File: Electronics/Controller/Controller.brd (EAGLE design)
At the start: 190 x 90 mm, 20 parts, among them Q1 IRFD9014, U1 GY-521MPU6050, X1 Battery, X2 Switch

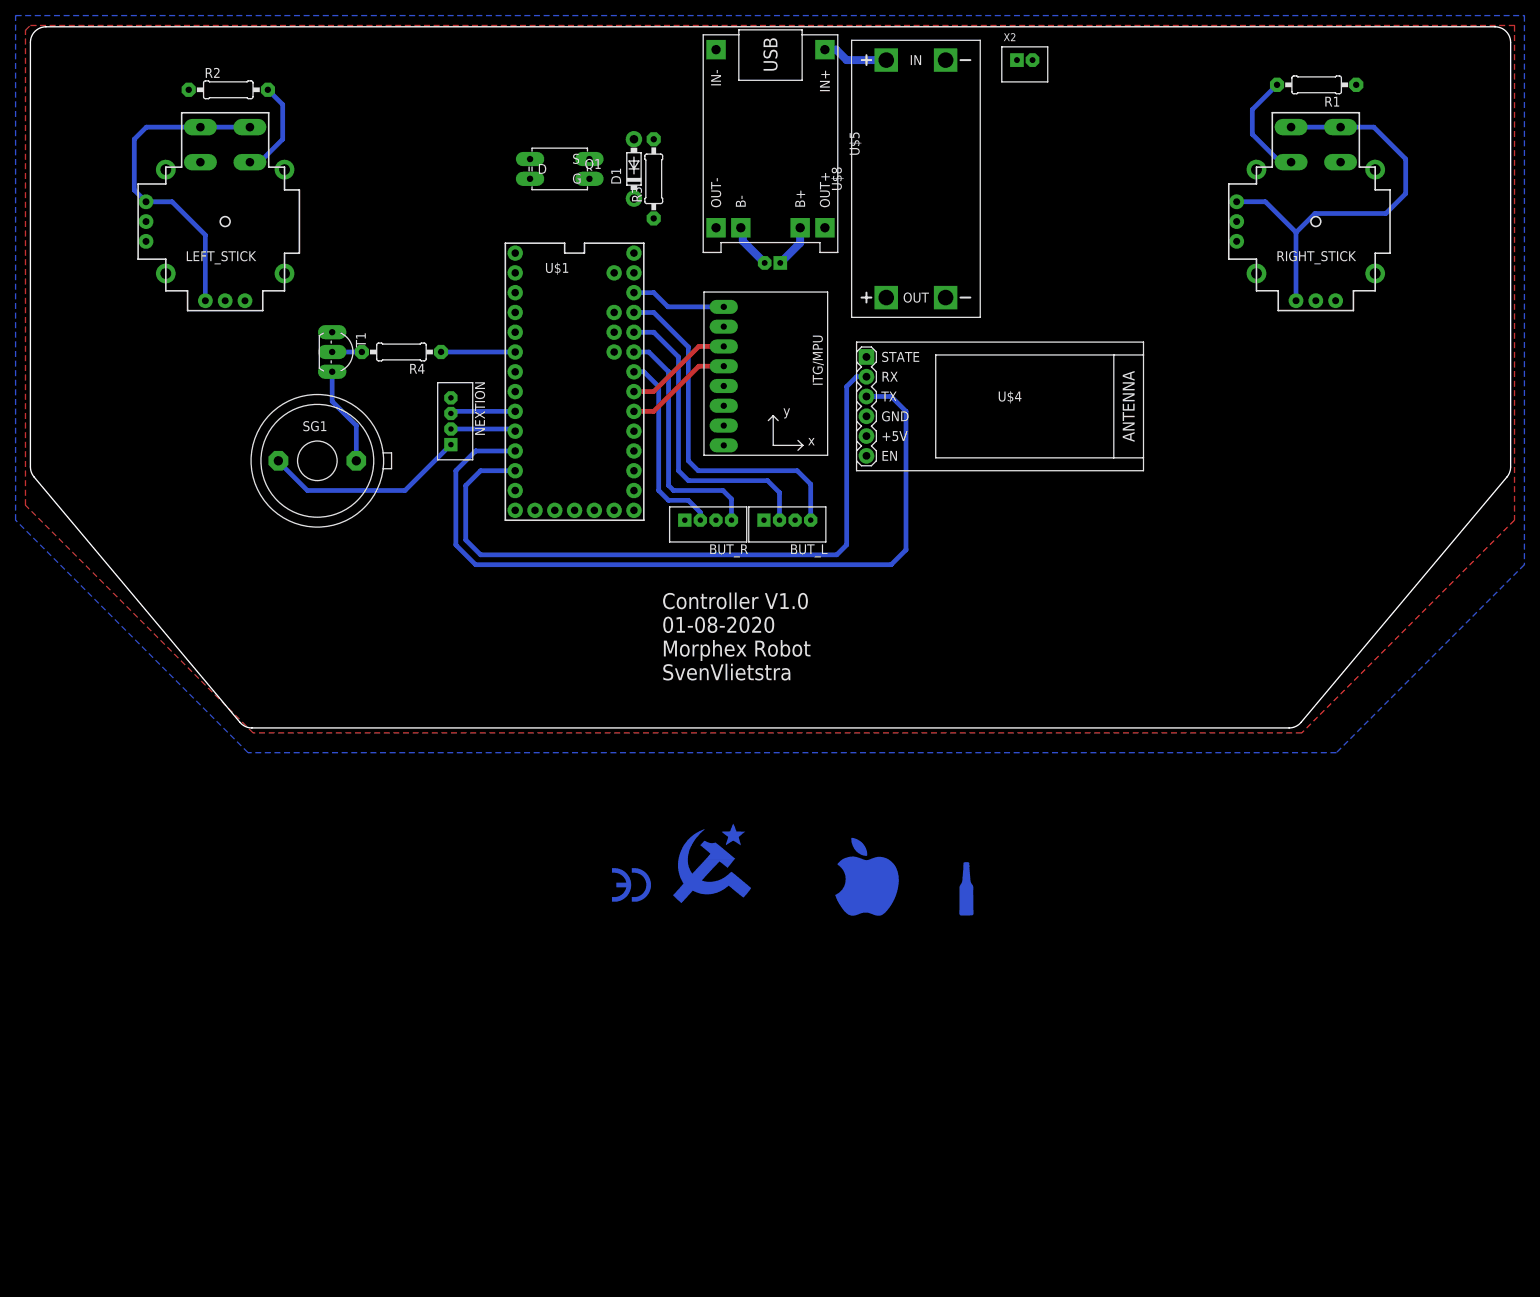
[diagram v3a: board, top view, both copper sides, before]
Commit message: Completed all routes
Completed all routes and changed the P-Channel mosfet to a NDP6020P
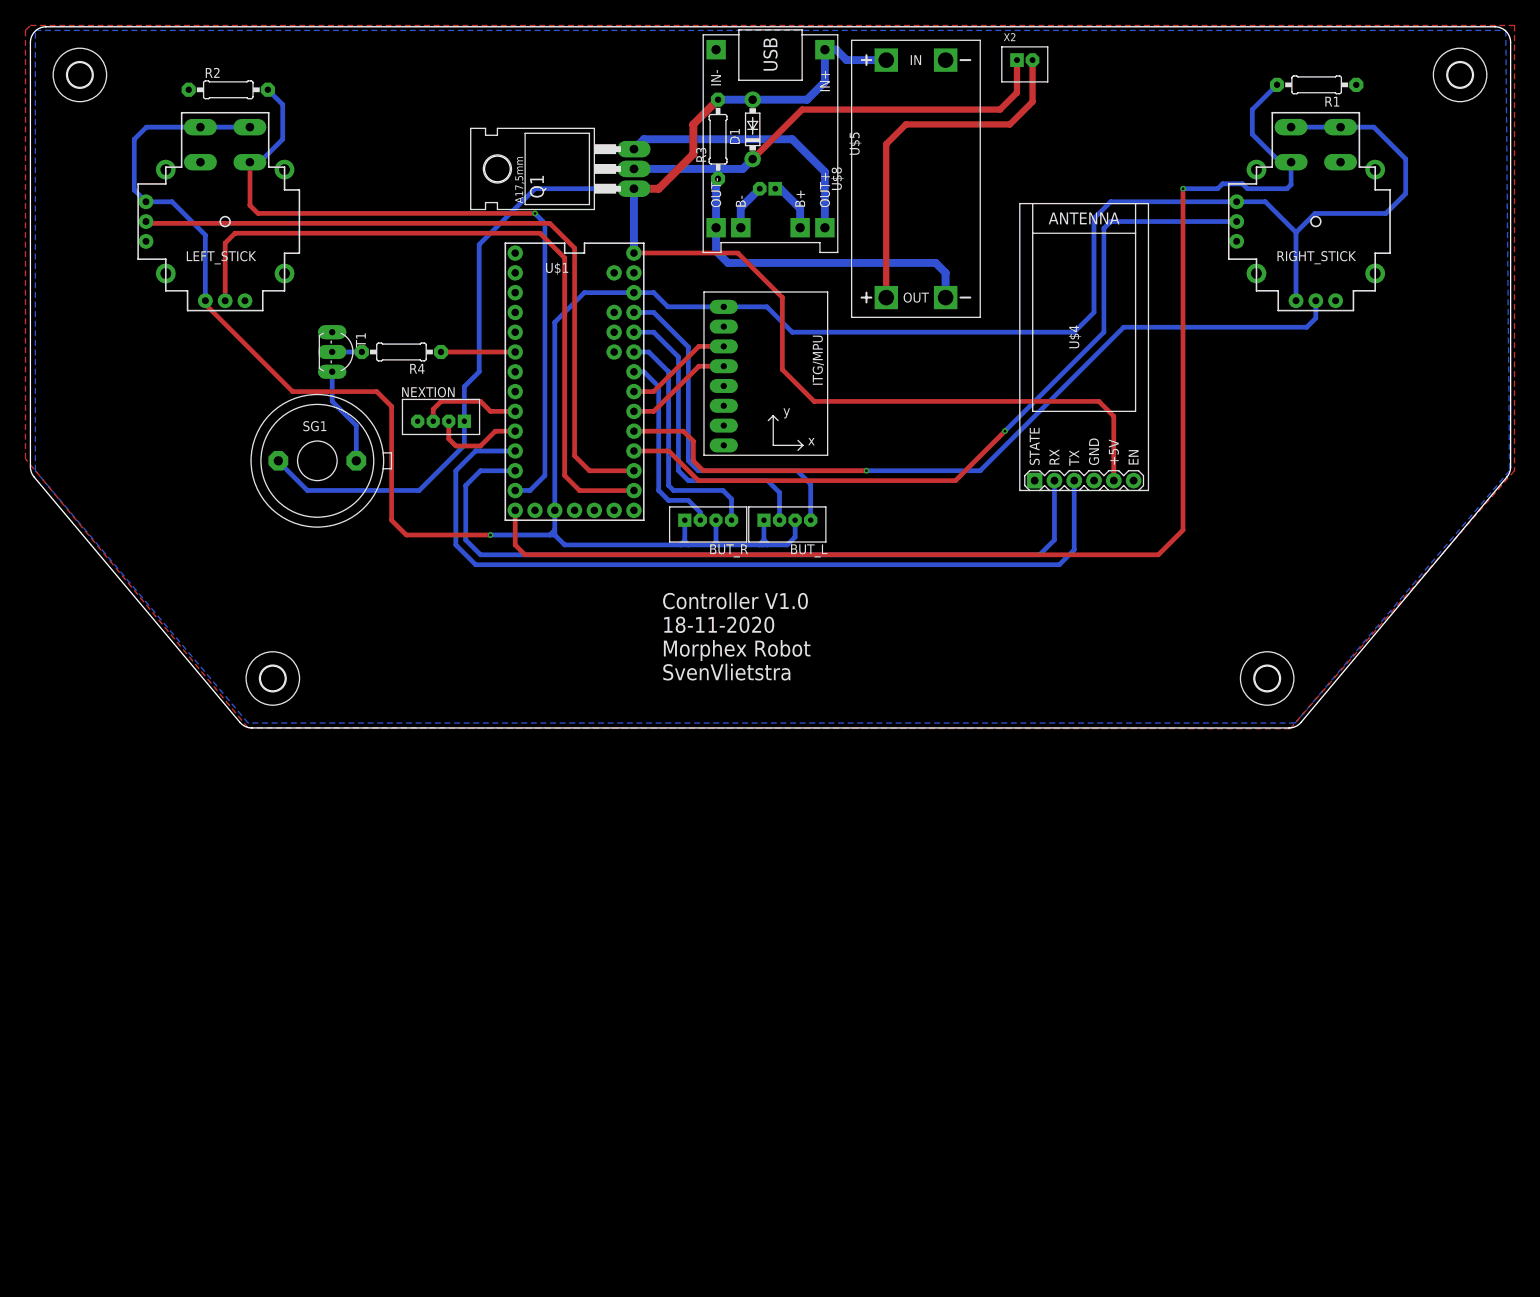
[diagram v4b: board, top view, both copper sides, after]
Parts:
- added U$2, U$3, U$6, U$7: (no value), holes:3,2
- Q1: value IRFD9014 -> (none); device transistor-small-signal:C370-01 -> transistor-power:TO220BH
- moved D1 16.1 mm to (92.7, 76.8)
- moved U$4 13.2 mm to (135.3, 48.9), turned to 0 degrees
- moved R3 9.69 mm to (88.3, 75.6)
- moved X1 9.55 mm to (94.6, 69.2)
- moved Q1 3.18 mm to (71.1, 71.8), turned to 90 degrees
- moved NEXTION 1.27 mm to (52.7, 39.4), turned to 0 degrees
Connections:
- new net SW2: R1.2, RIGHT_STICK.B2A, RIGHT_STICK.B2B, U$1.12
- net N$4: no longer Q1.D1
- net SW1: no longer R1.2, RIGHT_STICK.B2A, RIGHT_STICK.B2B, U$1.12
- net X-AXIS1: now also U$1.15/A1; no longer U$1.14/A0
- net Y-AXIS1: now also U$1.14/A0; no longer U$1.15/A1
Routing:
- net +3V3: track 109.2 -> 343.3 mm, vias 0 -> 1
- net +5V: track 34.6 -> 214.5 mm
- net SW2: track 0.00 -> 167.4 mm, vias 0 -> 1
- net Y-AXIS2: track 0.00 -> 101.5 mm, vias 0 -> 1
- net X-AXIS2: track 0.00 -> 100.5 mm, vias 0 -> 1
- net X-AXIS1: track 0.00 -> 91.5 mm
- net Y-AXIS1: track 0.00 -> 90.4 mm
- net SW1: track 26.7 -> 93.9 mm, vias 0 -> 1
- net N$4: track 0.00 -> 57.4 mm
- net N$6: track 0.00 -> 46.1 mm
- net N$1: track 0.00 -> 43.2 mm
- net N$5: track 0.00 -> 33.9 mm
- net BL_RX: track 87.7 -> 98.9 mm
- net BL_TX: track 101.5 -> 108.3 mm
- net NEX_TX: track 8.36 -> 13.0 mm
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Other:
- board text added: "Controller V1.0 18-11-2020 Morphex Robot SvenVlietstra"
- board text removed: "Controller V1.0 01-08-2020 Morphex Robot SvenVlietstra"

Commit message: Added Nextion in Board Layout
Added nextion in board layout and made the height 10mm for a standoff. Changed de JST connectors from 2mm to 2,54 spacing
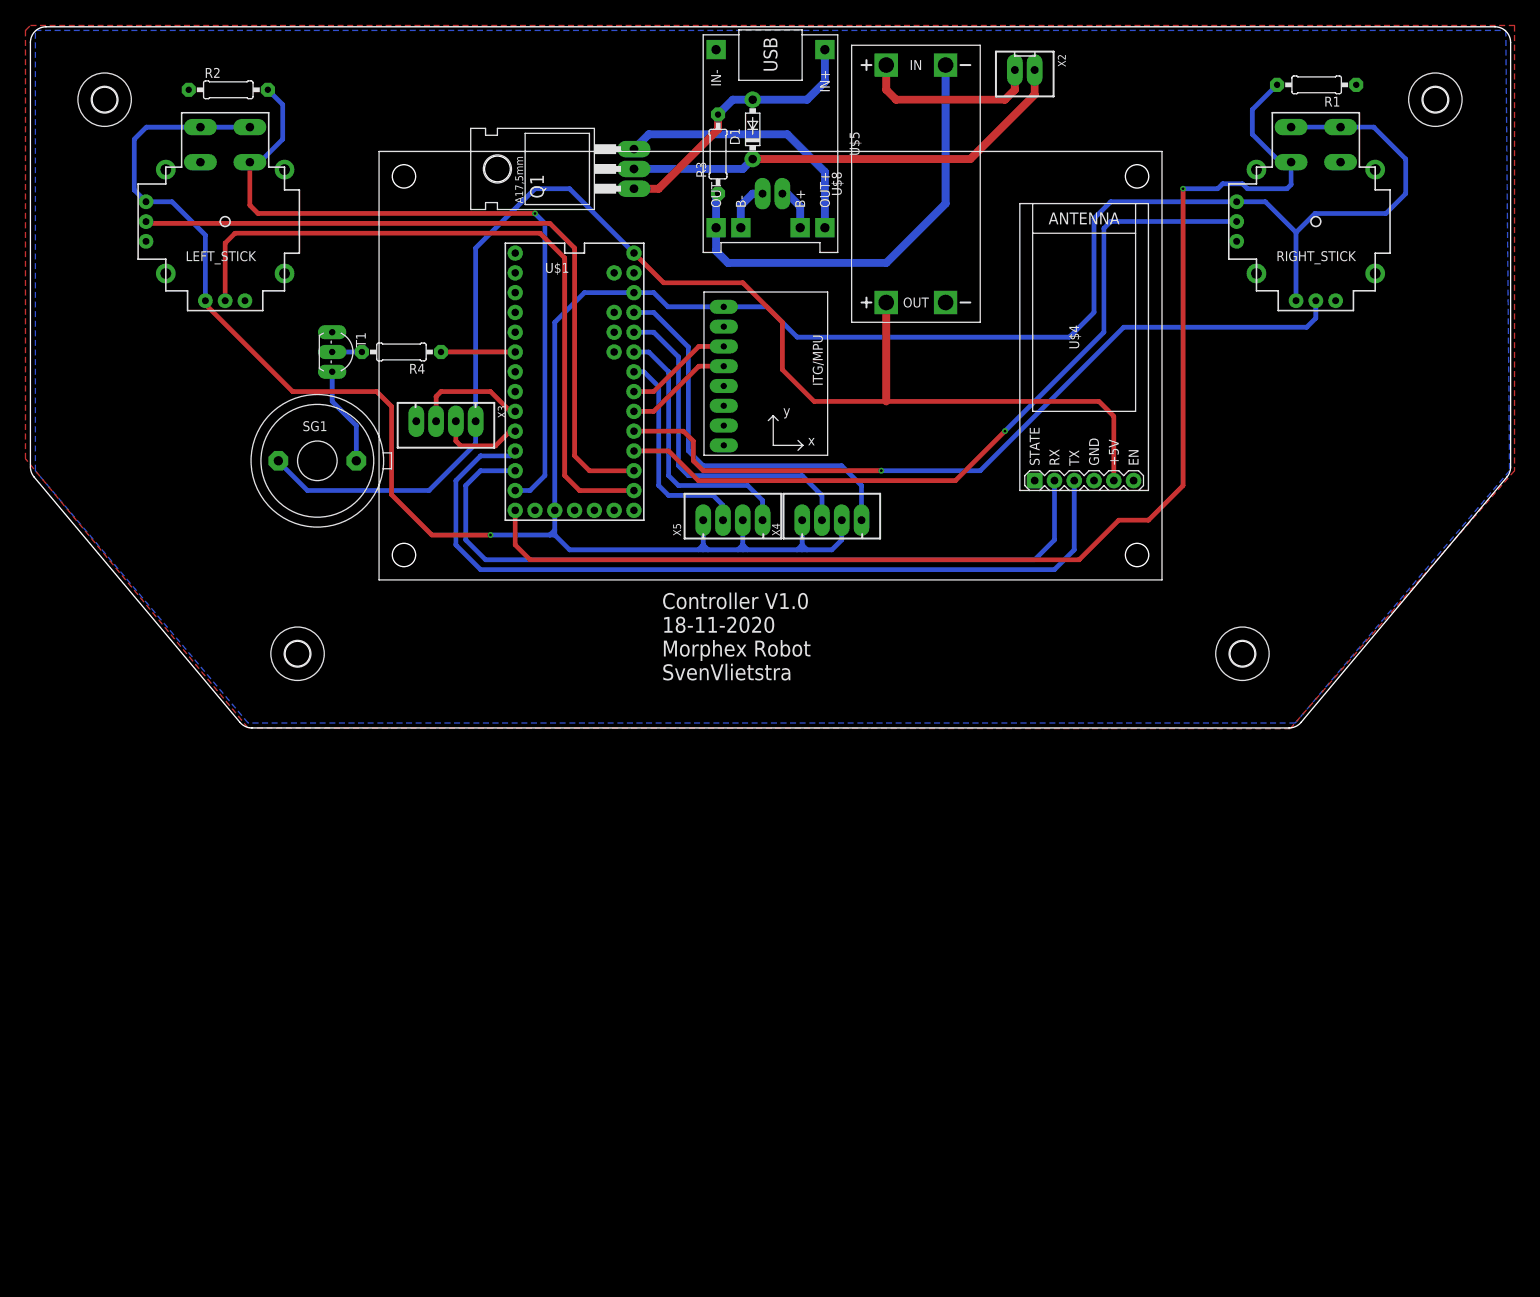
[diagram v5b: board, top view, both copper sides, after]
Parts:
- removed BUT_L, BUT_R, NEXTION: B4B-PH-K-S, con-JST PH:B4B-PH-K-S
- added U$9: NX4832K035, Nextion:NX4832K035
- added X3: Nextion, Rembrandt Electronics - JST XH Connectors v1-0:JST-XH-04-PACKAGE-LONG-PAD
- added X4: BUT_L, Rembrandt Electronics - JST XH Connectors v1-0:JST-XH-04-PACKAGE-LONG-PAD
- added X5: BUT_R, Rembrandt Electronics - JST XH Connectors v1-0:JST-XH-04-PACKAGE-LONG-PAD
- X1, X2: device con-JST PH:B2B-PH-K-S -> Rembrandt Electronics - JST XH Connectors v1-0:JST-XH-02-PACKAGE-LONG-PAD
- moved U$7 4.49 mm to (155.6, 9.53)
- moved U$6 4.49 mm to (34.3, 9.53)
- moved U$2 4.49 mm to (9.53, 80.6)
- moved U$3 4.49 mm to (180.3, 80.6)
- moved R3 1.91 mm to (88.3, 73.7)
- moved X2 1.27 mm to (127.6, 84.5)
- moved X1 0.90 mm to (95.2, 68.6), turned to 0 degrees
- moved U$8 0.64 mm to (113.7, 69.8)
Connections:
- new net N$9: D1.A, Q1.G, R3.2, U$5.IN+
- net +3V3: now also X4.1, X4.3, X5.1, X5.3; no longer BUT_L.1, BUT_L.3, BUT_R.1, BUT_R.3
- net +5V: now also U$8.OUT+, X3.1; no longer D1.A, NEXTION.1, Q1.G, R3.2, U$5.IN+, U$8.IN+
- net BUT_1: now also X4.2; no longer BUT_L.2
- net BUT_2: now also X4.4; no longer BUT_L.4
- net BUT_3: now also X5.2; no longer BUT_R.2
- net BUT_4: now also X5.4; no longer BUT_R.4
- net GND: now also U$8.OUT-, X3.4; no longer NEXTION.4, U$5.IN-, U$8.IN-
- net N$1: now also U$8.IN-; no longer U$8.OUT-
- net N$6: now also U$8.IN+; no longer U$8.OUT+
- net NEX_RX: now also X3.2; no longer NEXTION.2
- net NEX_TX: now also X3.3; no longer NEXTION.3
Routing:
- net +5V: track 214.5 -> 176.2 mm
- net N$9: track 0.00 -> 35.6 mm
- net N$6: track 46.1 -> 23.3 mm
- net N$1: track 43.2 -> 58.5 mm
- net +3V3: track 343.3 -> 352.6 mm
- net BUT_2: track 45.0 -> 50.7 mm
- net BUT_1: track 39.3 -> 44.2 mm
- net BUT_4: track 31.6 -> 34.8 mm
- net BUT_3: track 24.8 -> 27.9 mm
- net SW2: track 167.4 -> 164.6 mm
- net NEX_TX: track 13.0 -> 14.7 mm
- net N$4: track 57.4 -> 58.6 mm
- net N$2: track 6.70 -> 5.69 mm
- net NEX_RX: track 12.0 -> 11.2 mm
- net N$5: track 33.9 -> 34.5 mm
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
